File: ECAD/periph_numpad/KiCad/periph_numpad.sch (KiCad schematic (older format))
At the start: 0 parts

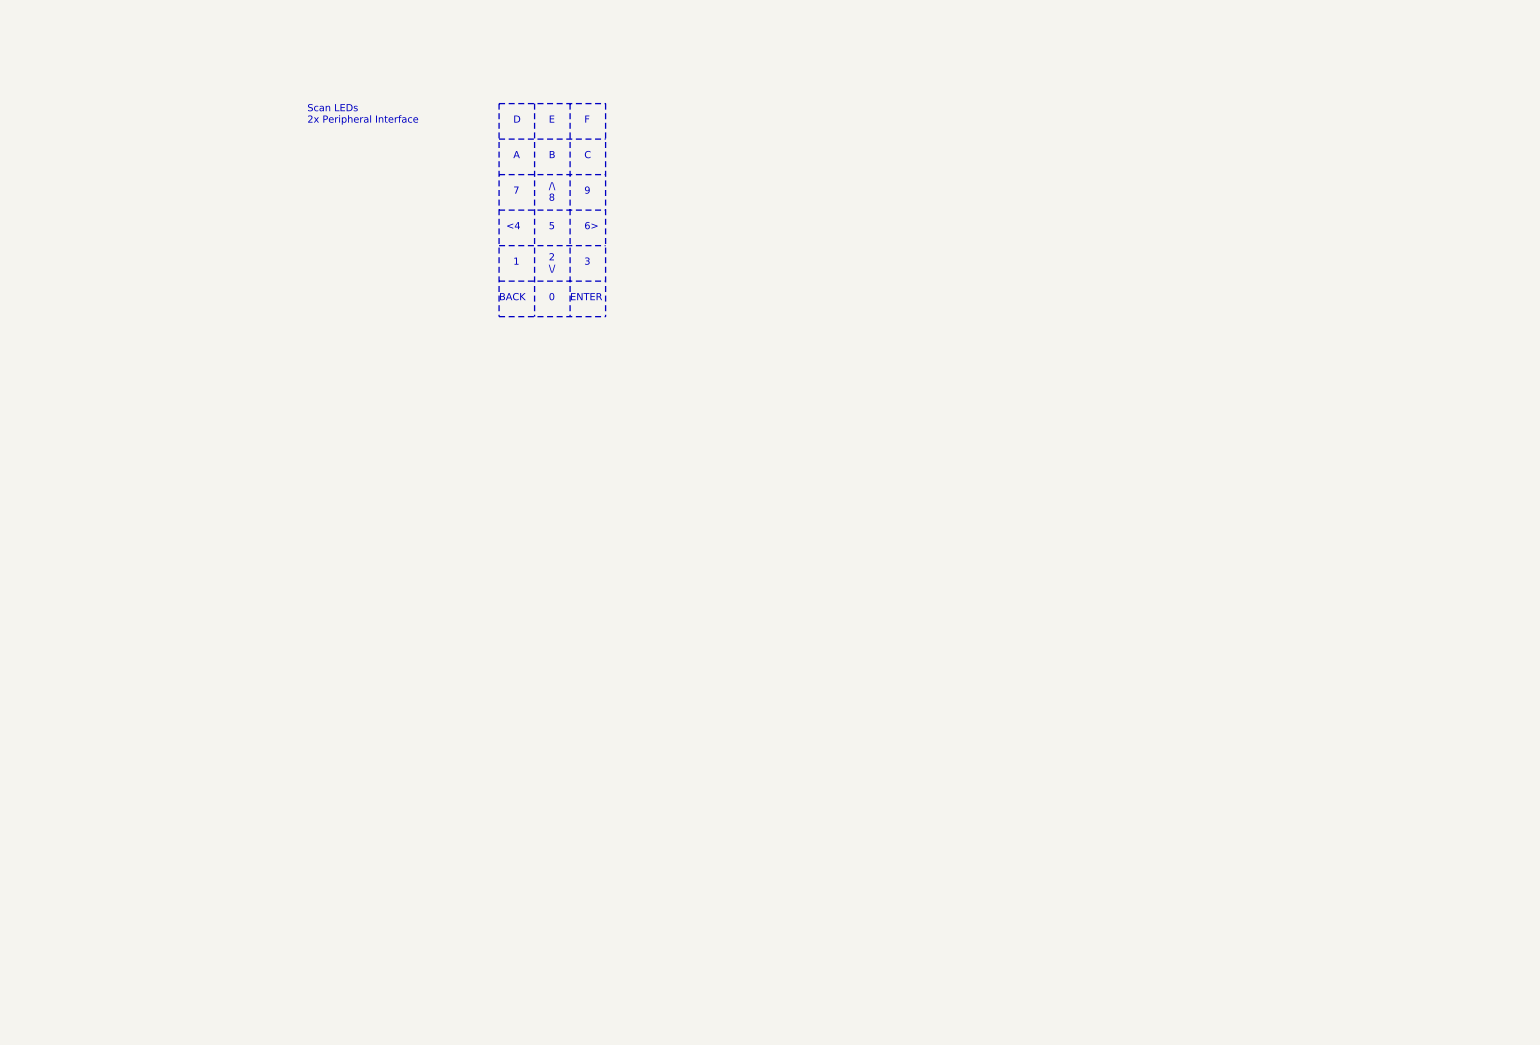
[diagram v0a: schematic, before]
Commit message: Numpad: Schematic done + parts placed
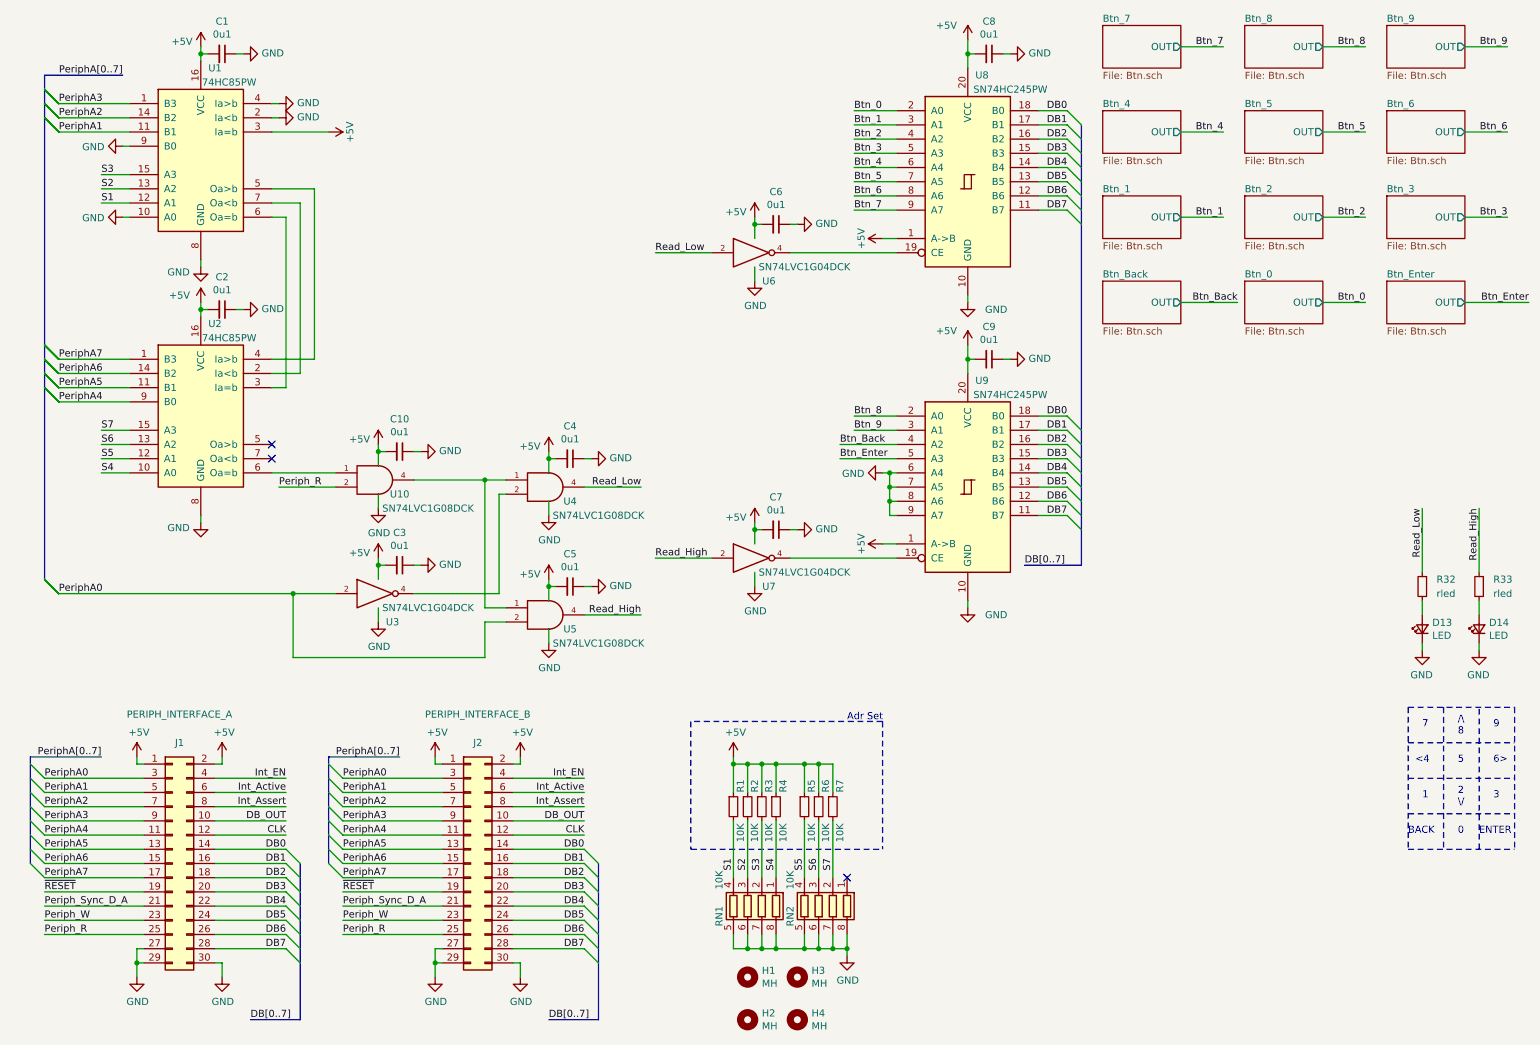
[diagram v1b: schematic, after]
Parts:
- added C1, C10, C2, C3, C4, C5, C6, C7, C8, C9: 0u1, NoRef_Footprints:C_0603_1608Metric_NoRef, symbol Device:C_Small
- added D13, D14: LED, NoRef_Footprints:D_0603_1608Metric_NoRef, symbol Device:LED_Small
- added H1, H2, H3, H4: MH, MountingHole:MountingHole_3.2mm_M3_Pad_Via, symbol Mechanical:MountingHole
- added J1: PERIPH_INTERFACE_A, Connector_IDC:IDC-Header_2x15_P2.54mm_Vertical, symbol Connector_Generic:Conn_02x15_Odd_Even
- added J2: PERIPH_INTERFACE_B, Connector_IDC:IDC-Header_2x15_P2.54mm_Vertical, symbol Connector_Generic:Conn_02x15_Odd_Even
- added R1, R2, R3, R4, R5, R6, R7: 10K, NoRef_Footprints:R_0603_1608Metric_NoRef, symbol Device:R_Small
- added R32, R33: rled, NoRef_Footprints:R_0603_1608Metric_NoRef, symbol Device:R_Small
- added RN1, RN2: 10K, NoRef_Footprints:R_Array_Convex_4x0603_NoRef, symbol Device:R_Pack04
- added U1, U2: 74HC85PW, Package_SO:TSSOP-16_4.4x5mm_P0.65mm, symbol 74xx:74LS85
- added U10, U4, U5: SN74LVC1G08DCK, Package_TO_SOT_SMD:SOT-353_SC-70-5, symbol 74xGxx:74LVC1G08
- added U3, U6, U7: SN74LVC1G04DCK, Package_TO_SOT_SMD:SOT-353_SC-70-5, symbol 74xGxx:74LVC1G04
- added U8, U9: SN74HC245PW, Package_SO:TSSOP-20_4.4x6.5mm_P0.65mm, symbol 74xx:74HC245
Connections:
- new net: U6.4, U8.19 (CE)
- new net: U10.4, U4.1, U5.1
- new net: U3.4, U4.2
- new net: U1.7 (Oa<b), U2.2 (Ia<b)
- new net: U1.6 (Oa=b), U2.3 (Ia=b)
- new net: U1.5 (Oa>b), U2.4 (Ia>b)
- new net: U10.1, U2.6 (Oa=b)
- new net: U7.4, U9.19 (CE)
- new net: D13.2 (A), R32.2
- new net: D14.2 (A), R33.2
- new net +5V: C1.2, C10.2, C2.2, C3.2, C4.2, C5.2, C6.2, C7.2, C8.2, C9.2, J1.1 (Pin_1), J1.2 (Pin_2), J2.1 (Pin_1), J2.2 (Pin_2), R1.1, R2.1, R3.1, R4.1, R5.1, R6.1, R7.1, U1.16 (VCC), U1.3 (Ia=b), U10.5 (VCC), U2.16 (VCC), U3.5 (VCC), U4.5 (VCC), U5.5 (VCC), U6.5 (VCC), U7.5 (VCC), U8.1 (A->B), U8.20 (VCC), U9.1 (A->B), U9.20 (VCC)
- new net Btn_0: U8.2 (A0)
- new net Btn_1: U8.3 (A1)
- new net Btn_2: U8.4 (A2)
- new net Btn_3: U8.5 (A3)
- new net Btn_4: U8.6 (A4)
- new net Btn_5: U8.7 (A5)
- new net Btn_6: U8.8 (A6)
- new net Btn_7: U8.9 (A7)
- new net Btn_8: U9.2 (A0)
- new net Btn_9: U9.3 (A1)
- new net Btn_Back: U9.4 (A2)
- new net Btn_Enter: U9.5 (A3)
- new net CLK: J1.12 (Pin_12), J2.12 (Pin_12)
- new net DB0: J1.14 (Pin_14), J2.14 (Pin_14), U8.18 (B0), U9.18 (B0)
- new net DB1: J1.16 (Pin_16), J2.16 (Pin_16), U8.17 (B1), U9.17 (B1)
- new net DB2: J1.18 (Pin_18), J2.18 (Pin_18), U8.16 (B2), U9.16 (B2)
- new net DB3: J1.20 (Pin_20), J2.20 (Pin_20), U8.15 (B3), U9.15 (B3)
- new net DB4: J1.22 (Pin_22), J2.22 (Pin_22), U8.14 (B4), U9.14 (B4)
- new net DB5: J1.24 (Pin_24), J2.24 (Pin_24), U8.13 (B5), U9.13 (B5)
- new net DB6: J1.26 (Pin_26), J2.26 (Pin_26), U8.12 (B6), U9.12 (B6)
- new net DB7: J1.28 (Pin_28), J2.28 (Pin_28), U8.11 (B7), U9.11 (B7)
- new net DB_OUT: J1.10 (Pin_10), J2.10 (Pin_10)
- new net GND: C1.1, C10.1, C2.1, C3.1, C4.1, C5.1, C6.1, C7.1, C8.1, C9.1, D13.1 (K), D14.1 (K), J1.27 (Pin_27), J1.29 (Pin_29), J1.30 (Pin_30), J2.27 (Pin_27), J2.29 (Pin_29), J2.30 (Pin_30), RN1.5 (R4.2), RN1.6 (R3.2), RN1.7 (R2.2), RN1.8 (R1.2), RN2.5 (R4.2), RN2.6 (R3.2), RN2.7 (R2.2), RN2.8 (R1.2), U1.10 (A0), U1.2 (Ia<b), U1.4 (Ia>b), U1.8 (GND), U1.9 (B0), U10.3 (GND), U2.8 (GND), U3.3 (GND), U4.3 (GND), U5.3 (GND), U6.3 (GND), U7.3 (GND), U8.10 (GND), U9.10 (GND), U9.6 (A4), U9.7 (A5), U9.8 (A6), U9.9 (A7)
- new net Int_Active: J1.6 (Pin_6), J2.6 (Pin_6)
- new net Int_Assert: J1.8 (Pin_8), J2.8 (Pin_8)
- new net Int_EN: J1.4 (Pin_4), J2.4 (Pin_4)
- new net PeriphA0: J1.3 (Pin_3), J2.3 (Pin_3), U3.2, U5.2
- new net PeriphA1: J1.5 (Pin_5), J2.5 (Pin_5), U1.11 (B1)
- new net PeriphA2: J1.7 (Pin_7), J2.7 (Pin_7), U1.14 (B2)
- new net PeriphA3: J1.9 (Pin_9), J2.9 (Pin_9), U1.1 (B3)
- new net PeriphA4: J1.11 (Pin_11), J2.11 (Pin_11), U2.9 (B0)
- new net PeriphA5: J1.13 (Pin_13), J2.13 (Pin_13), U2.11 (B1)
- new net PeriphA6: J1.15 (Pin_15), J2.15 (Pin_15), U2.14 (B2)
- new net PeriphA7: J1.17 (Pin_17), J2.17 (Pin_17), U2.1 (B3)
- new net Periph_R: J1.25 (Pin_25), J2.25 (Pin_25), U10.2
- new net Periph_Sync_D_A: J1.21 (Pin_21), J2.21 (Pin_21)
- new net Periph_W: J1.23 (Pin_23), J2.23 (Pin_23)
- new net Read_High: R33.1, U5.4, U7.2
- new net Read_Low: R32.1, U4.4, U6.2
- new net S1: R1.2, RN1.4 (R4.1), U1.12 (A1)
- new net S2: R2.2, RN1.3 (R3.1), U1.13 (A2)
- new net S3: R3.2, RN1.2 (R2.1), U1.15 (A3)
- new net S4: R4.2, RN1.1 (R1.1), U2.10 (A0)
- new net S5: R5.2, RN2.4 (R4.1), U2.12 (A1)
- new net S6: R6.2, RN2.3 (R3.1), U2.13 (A2)
- new net S7: R7.2, RN2.2 (R2.1), U2.15 (A3)
- new net ~RESET: J1.19 (Pin_19), J2.19 (Pin_19)
- no-connect marks 0 -> 3
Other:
- note added: "Adr Set"
- note removed: "A"
- note removed: "B"
- note removed: "C"
- note removed: "D"
- note removed: "E"
- note removed: "F"
- note removed: "Scan LEDs\n2x Peripheral Interface"
